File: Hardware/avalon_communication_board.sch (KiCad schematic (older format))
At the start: 17 parts, among them P1 B2P-VH, Q1 FMMT597, Q2 BC817, Q3 BC817, Q4 FMMT597, Q5 BC817

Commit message: -Ethernet controller schematic complete -Ferrite Bead component changed -Components selected and added to the communications board BOM, located in Google Drive -Filter Capacitor values changed to recommended values from Ethernet Controller datasheet
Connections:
- net DUE144 renamed ULTRA_CTR
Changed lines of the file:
@@
 Connection ~ 2460 3910
 Text GLabel 3930 4340 2    60   Input ~ 0
-DUE144
+ULTRA_CTR
 Wire Wire Line
 	740  4340 3930 4340

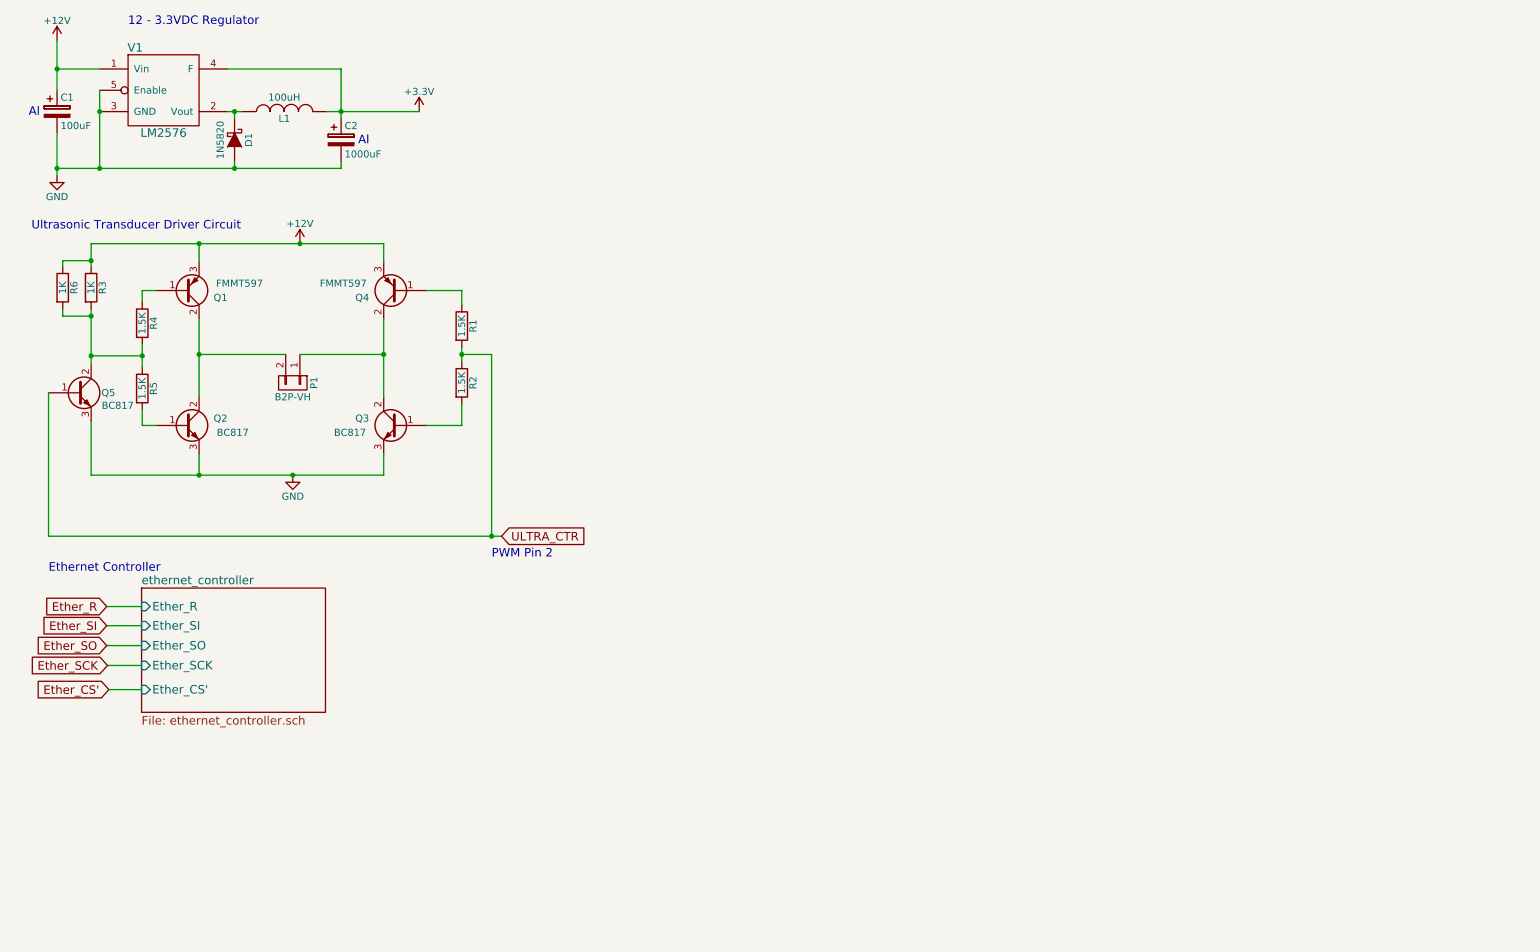
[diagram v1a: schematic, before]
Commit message: -Added Main Due Connector, 12 - 5V Regulator, I2C Bus Connections
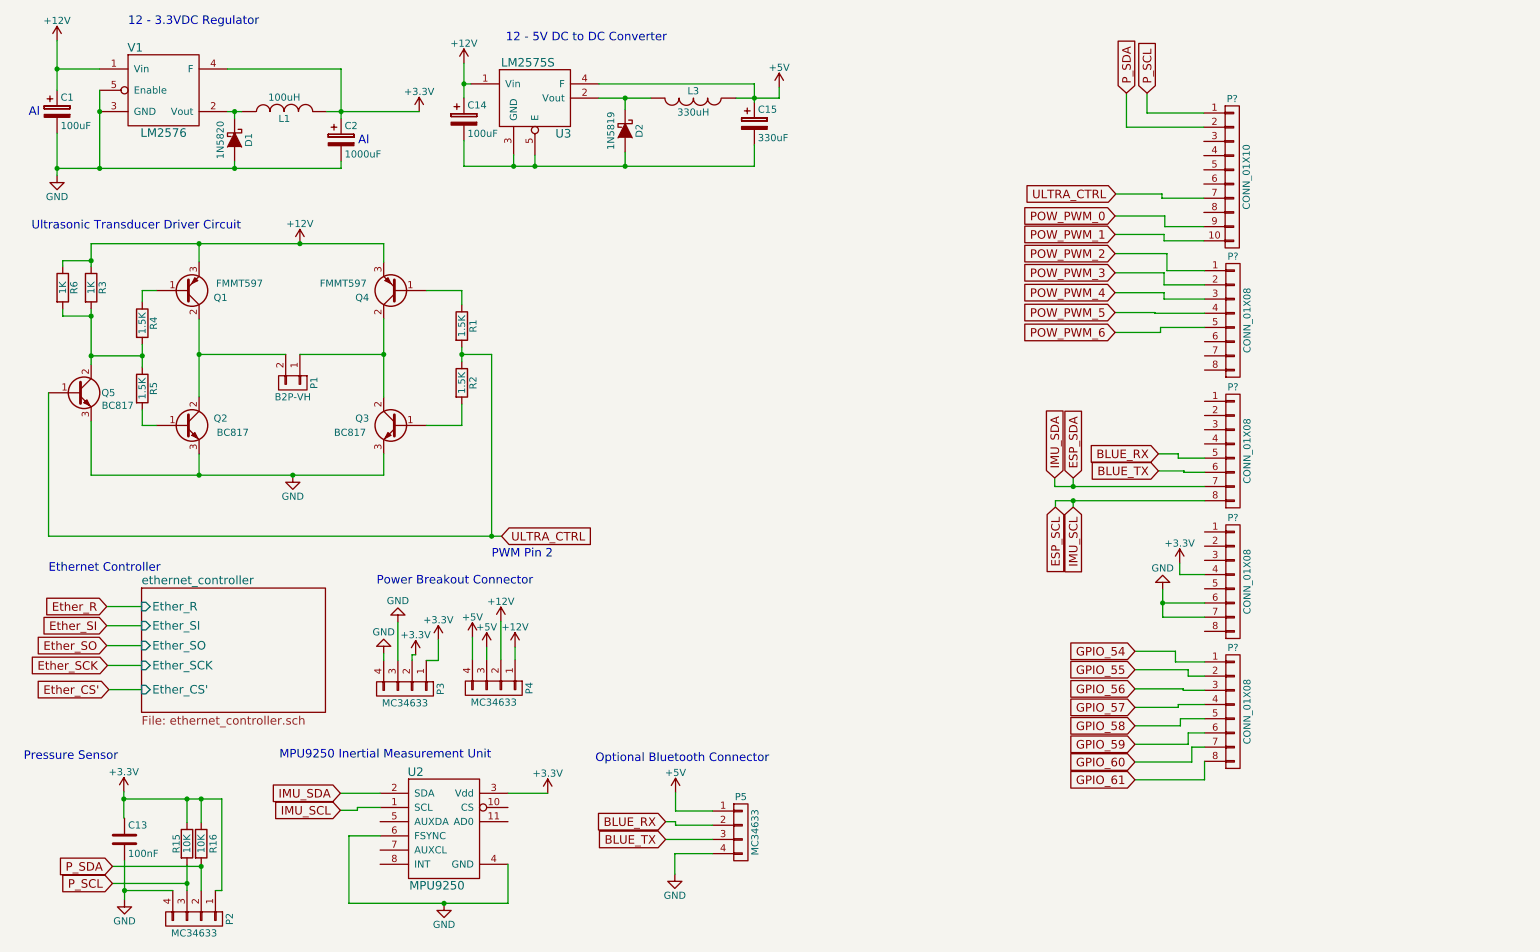
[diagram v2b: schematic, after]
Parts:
- added C13: 100nF, symbol C
- added C14: 100uF, symbol CP
- added C15: 330uF, symbol CP
- added D2: 1N5819, symbol D_Schottky
- added L3: 330uH, symbol INDUCTOR
- added P2, P3, P4, P5: MC34633, symbol CONN_01X04
- added P?: CONN_01X10, symbol CONN_01X10
- added P? (x4): CONN_01X08, symbol CONN_01X08
- added R15, R16: 10K, symbol R
- added U2: MPU9250, symbol MPU9250
- added U3: LM2575S, symbol LM2575S
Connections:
- net +12V: now also C14.1, P4.1 (P1), P4.2 (P2), U3.1 (Vin)
- net +3V3: now also P2.1 (P1), P3.1 (P1), P3.2 (P2), P?.4 (P4), R15.1, R16.1, U2.3 (Vdd)
- net GND: now also C13.2, P2.4 (P4), P3.3 (P3), P3.4 (P4), P5.4 (P4), P?.6 (P6), P?.7 (P7), U2.4 (GND), U2.6 (FSYNC)
- net ULTRA_CTR renamed ULTRA_CTRL
- net ULTRA_CTRL: now also P?.7 (P7)
- new net: D2.1 (K), L3.2, U3.2 (Vout)
- new net: C14.2, C15.2, D2.2 (A), U3.3 (GND), U3.5 (E)
- new net +5V: C15.1, L3.1, P4.3 (P3), P4.4 (P4), P5.1 (P1), U3.4 (F)
- new net BLUE_RX: P5.2 (P2), P?.5 (P5)
- new net BLUE_TX: P5.3 (P3), P?.6 (P6)
- new net ESP_SCL: P?.8 (P8), U2.1 (SCL)
- new net ESP_SDA: P?.7 (P7), U2.2 (SDA)
- new net GPIO_54: P?.1 (P1)
- new net GPIO_55: P?.2 (P2)
- new net GPIO_56: P?.3 (P3)
- new net GPIO_57: P?.4 (P4)
- new net GPIO_58: P?.5 (P5)
- new net GPIO_59: P?.6 (P6)
- new net GPIO_60: P?.7 (P7)
- new net GPIO_61: P?.8 (P8)
- new net POW_PWM_0: P?.9 (P9)
- new net POW_PWM_1: P?.10 (P10)
- new net POW_PWM_2: P?.1 (P1)
- new net POW_PWM_3: P?.2 (P2)
- new net POW_PWM_4: P?.3 (P3)
- new net POW_PWM_5: P?.4 (P4)
- new net POW_PWM_6: P?.5 (P5)
- new net P_SCL: P2.3 (P3), P?.1 (P1), R15.2
- new net P_SDA: P2.2 (P2), P?.2 (P2), R16.2
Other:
- note added: "12 - 5V DC to DC Converter"
- note added: "MPU9250 Inertial Measurement Unit"
- note added: "Optional Bluetooth Connector"
- note added: "Power Breakout Connector"
- note added: "Pressure Sensor"

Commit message: -Added the ESP8266 Microcontroller and support circuitry for programming
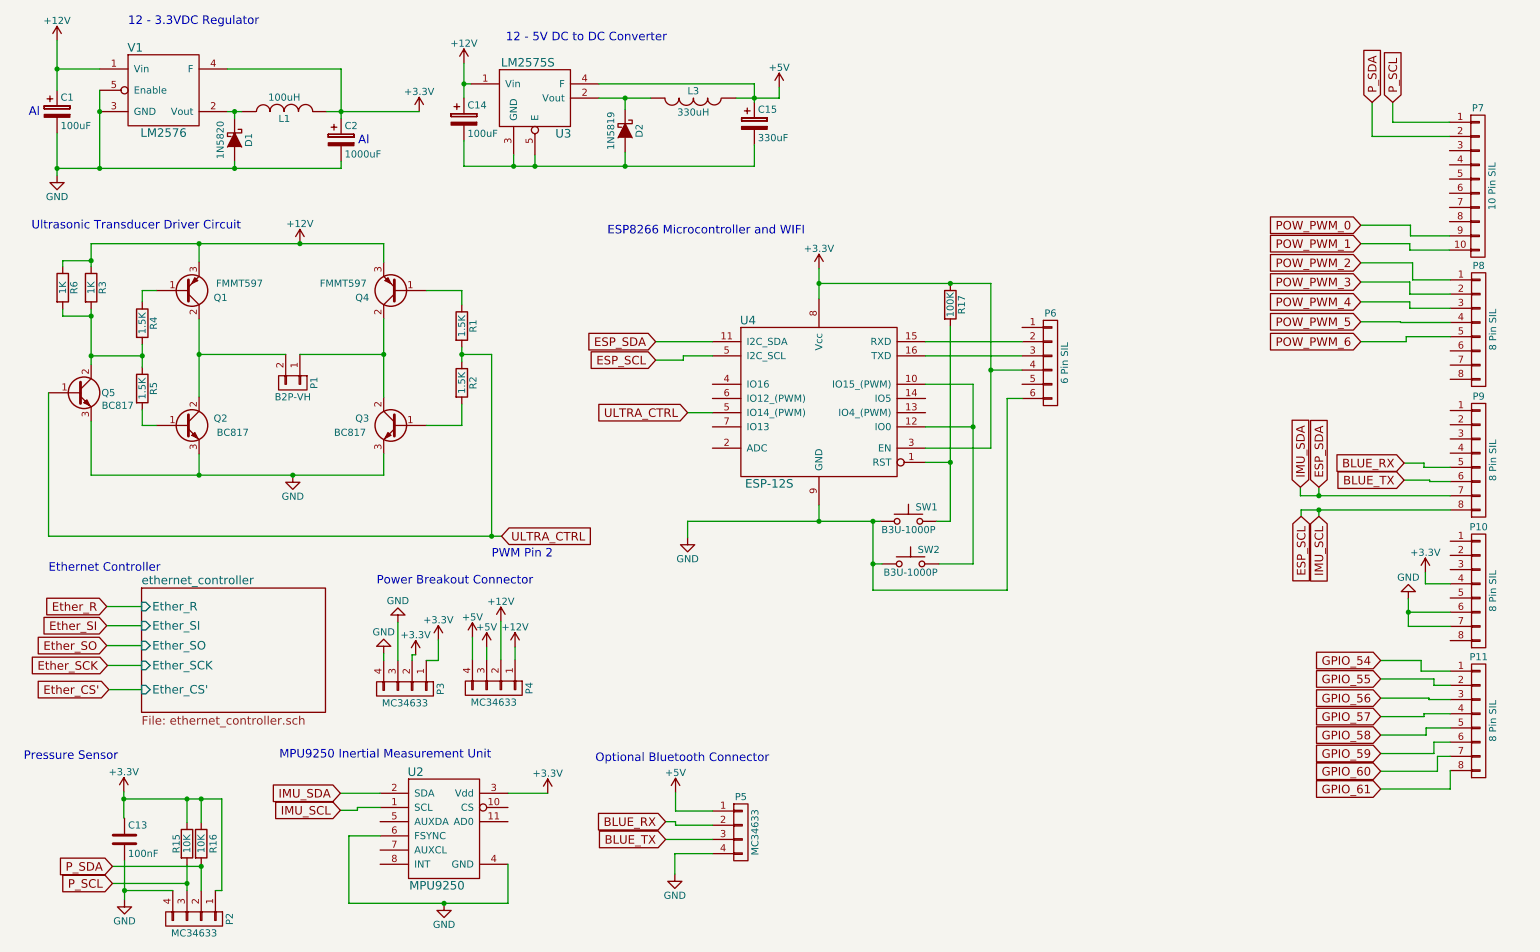
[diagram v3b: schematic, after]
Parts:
- added P6: 6 Pin SIL, symbol CONN_01X06
- added R17: 100K, symbol R
- added SW1, SW2: B3U-1000P, symbol SW_Push
- added U4: ESP-12S, symbol ESP-12S
- P10, P11, P8, P9: renamed from P?; value CONN_01X08 -> 8 Pin SIL
- P7: renamed from P?; value CONN_01X10 -> 10 Pin SIL
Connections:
- net +3V3: now also P6.4 (P4), R17.1, U4.3 (EN), U4.8 (Vcc)
- net ESP_SCL: now also U4.5 (IO14_(PWM))
- net ESP_SDA: now also U4.11 (I2C_SDA)
- net GND: now also P6.6 (P6), SW1.1, SW2.1, U4.9 (GND)
- net ULTRA_CTRL: now also U4.5 (IO14_(PWM)); no longer P7.7 (P7)
- new net: R17.2, SW1.2, U4.1 (RST)
- new net: SW2.2, U4.10 (IO15_(PWM)), U4.12 (IO0)
- new net: P6.2 (P2), U4.15 (RXD)
- new net: P6.3 (P3), U4.16 (TXD)
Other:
- note added: "ESP8266 Microcontroller and WIFI"
- moved on the sheet: P10, P11, P7, P8, P9

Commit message: -Arduino Due Connector completed
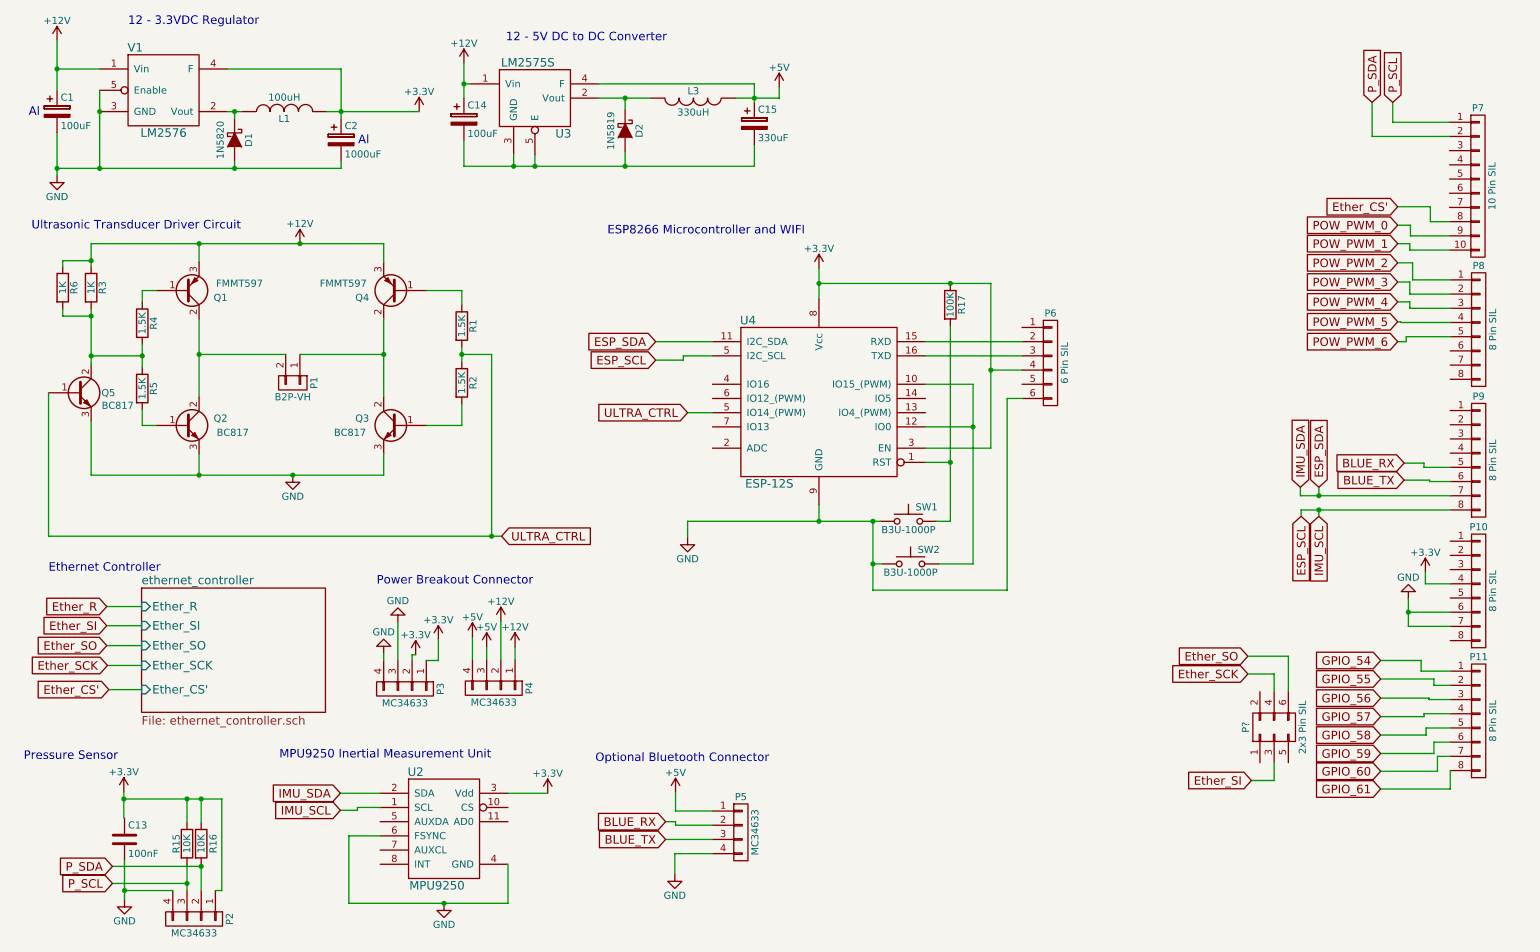
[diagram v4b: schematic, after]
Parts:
- added P?: 2x3 Pin SIL, symbol CONN_02X03
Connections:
- net Ether_CS': now also P7.8 (P8)
- net Ether_SCK: now also P?.4 (P4)
- net Ether_SI: now also P?.3 (P3)
- net Ether_SO: now also P?.6 (P6)
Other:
- note removed: "PWM Pin 2"
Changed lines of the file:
@@
 Text GLabel 3930 4340 2    60   Input ~ 0
 ULTRA_CTRL
-Text Notes 3860 4500 0    60   ~ 0
-PWM Pin 2
 Text Notes 620  2190 0    60   ~ 0
 Ultrasonic Transducer Driver Circuit
@@
 Text GLabel 10060 1285 1    60   Input ~ 0
 P_SDA
-Text GLabel 9980 2150 0    60   Input ~ 0
+Text GLabel 10240 2150 0    60   Input ~ 0
 POW_PWM_0
-Text GLabel 9980 2280 0    60   Input ~ 0
+Text GLabel 10240 2280 0    60   Input ~ 0
 POW_PWM_1
-Text GLabel 9980 2415 0    60   Input ~ 0
+Text GLabel 10240 2415 0    60   Input ~ 0
 POW_PWM_2
-Text GLabel 9980 2550 0    60   Input ~ 0
+Text GLabel 10240 2550 0    60   Input ~ 0
 POW_PWM_3
-Text GLabel 9980 2690 0    60   Input ~ 0
+Text GLabel 10240 2690 0    60   Input ~ 0
 POW_PWM_4
-Text GLabel 9980 2830 0    60   Input ~ 0
+Text GLabel 10240 2830 0    60   Input ~ 0
 POW_PWM_5
-Text GLabel 9980 2970 0    60   Input ~ 0
+Text GLabel 10240 2970 0    60   Input ~ 0
 POW_PWM_6
 Text GLabel 10285 3825 0    60   Input ~ 0
@@
 	10060 1525 10605 1525
 Wire Wire Line
-	9980 2150 10330 2150
-Wire Wire Line
 	10330 2150 10330 2225
 Wire Wire Line
 	10330 2225 10605 2225
 Wire Wire Line
-	9980 2280 10325 2280
-Wire Wire Line
 	10325 2280 10325 2325
 Wire Wire Line
 	10325 2325 10605 2325
 Wire Wire Line
-	9980 2415 10345 2415
-Wire Wire Line
 	10345 2415 10345 2535
 Wire Wire Line
 	10345 2535 10610 2535
 Wire Wire Line
-	9980 2550 10325 2550
-Wire Wire Line
 	10325 2550 10325 2635
 Wire Wire Line
 	10325 2635 10610 2635
 Wire Wire Line
-	9980 2690 10325 2690
-Wire Wire Line
 	10325 2690 10325 2735
 Wire Wire Line
 	10325 2735 10610 2735
 Wire Wire Line
-	9980 2830 10260 2830
-Wire Wire Line
 	10260 2830 10260 2835
 Wire Wire Line
 	10260 2835 10610 2835
-Wire Wire Line
-	9980 2970 10300 2970
 Wire Wire Line
 	10300 2970 10300 2935
@@
 Connection ~ 6545 4235
 Wire Wire Line
-	7375 3720 7375 2560
-Wire Wire Line
-	6915 3720 7375 3720
-Wire Wire Line
-	7375 2560 6165 2560
+	7375 2560 7375 3720
+Wire Wire Line
+	7375 3720 6915 3720
+Wire Wire Line
+	6165 2560 7375 2560
 Wire Wire Line
 	6545 4720 7490 4720
@@
 Text Notes 4675 2225 0    60   ~ 0
 ESP8266 Microcontroller and WIFI
+Wire Wire Line
+	10240 2150 10330 2150
+Wire Wire Line
+	10240 2280 10325 2280
+Wire Wire Line
+	10240 2415 10345 2415
+Wire Wire Line
+	10240 2550 10325 2550
+Wire Wire Line
+	10240 2690 10325 2690
+Wire Wire Line
+	10240 2830 10260 2830
+Wire Wire Line
+	10240 2970 10300 2970
+$Comp
+L CONN_02X03 P?
+U 1 1 5AA08E5D
+P 9370 5685
+F 0 "P?" H 9370 5885 50  0000 C CNN
+F 1 "2x3 Pin SIL" H 9370 5485 50  0000 C CNN
+F 2 "" H 9370 4485 50  0000 C CNN
+F 3 "" H 9370 4485 50  0000 C CNN
+	1    9370 5685
+	0    -1   -1   0
+$EndComp
+Text GLabel 9185 5185 0    60   Input ~ 0
+Ether_SO
+Text GLabel 9210 6060 0    60   Input ~ 0
+Ether_SI
+Text GLabel 9185 5310 0    60   Input ~ 0
+Ether_SCK
+Wire Wire Line
+	9185 5185 9470 5185
+Wire Wire Line
+	9470 5185 9470 5435
+Wire Wire Line
+	9185 5310 9370 5310
+Wire Wire Line
+	9370 5310 9370 5435
+Wire Wire Line
+	9210 6060 9370 6060
+Wire Wire Line
+	9370 6060 9370 5935
+Text GLabel 10240 2020 0    60   Input ~ 0
+Ether_CS'
+Wire Wire Line
+	10240 2020 10470 2020
+Wire Wire Line
+	10470 2020 10470 2125
+Wire Wire Line
+	10470 2125 10605 2125
 $EndSCHEMATC

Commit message: -Updates made to Arduino Due Connector -Updates made to Ultrasonic Transducer Control Circuit -Moved schematic sections around to make space -Added camera electronics sub sheet
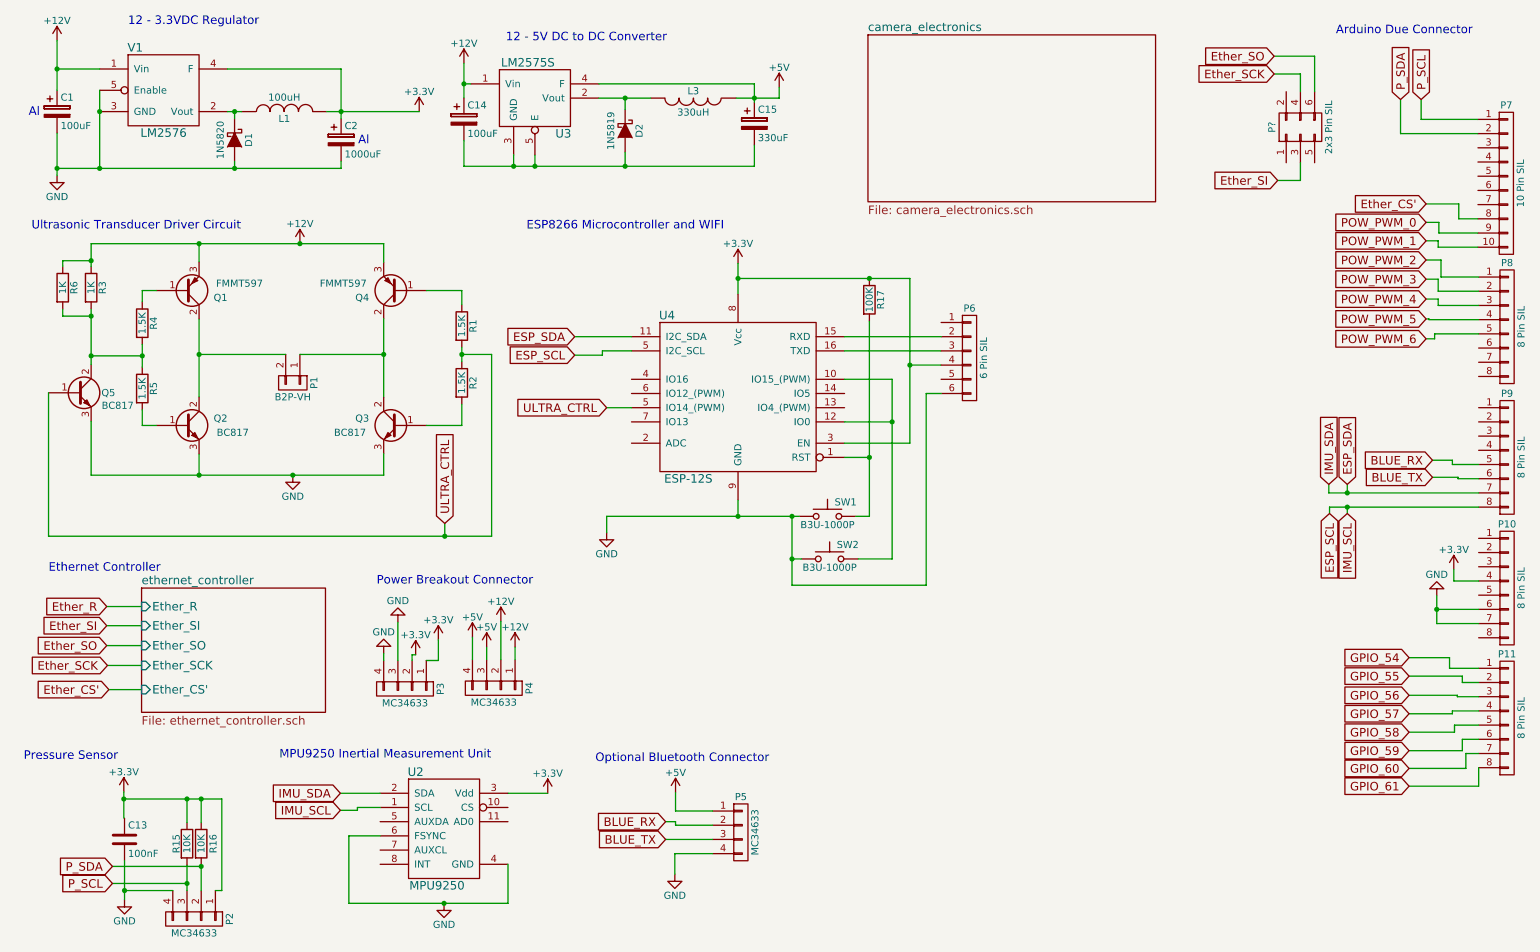
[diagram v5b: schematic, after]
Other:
- note added: "Arduino Due Connector"
- moved on the sheet: P10, P11, P6, P7, P8, P9, P?, R17, SW1, SW2, U4
